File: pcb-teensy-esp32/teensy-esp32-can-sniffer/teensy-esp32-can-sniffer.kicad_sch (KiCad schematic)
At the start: 21 parts, among them J1 Conn_01x04, U1 Seeed_Studio_XIAO_ESP32S3, U2 Teensy4.0, U3 TJA1051T-3, U4 AP63205WU

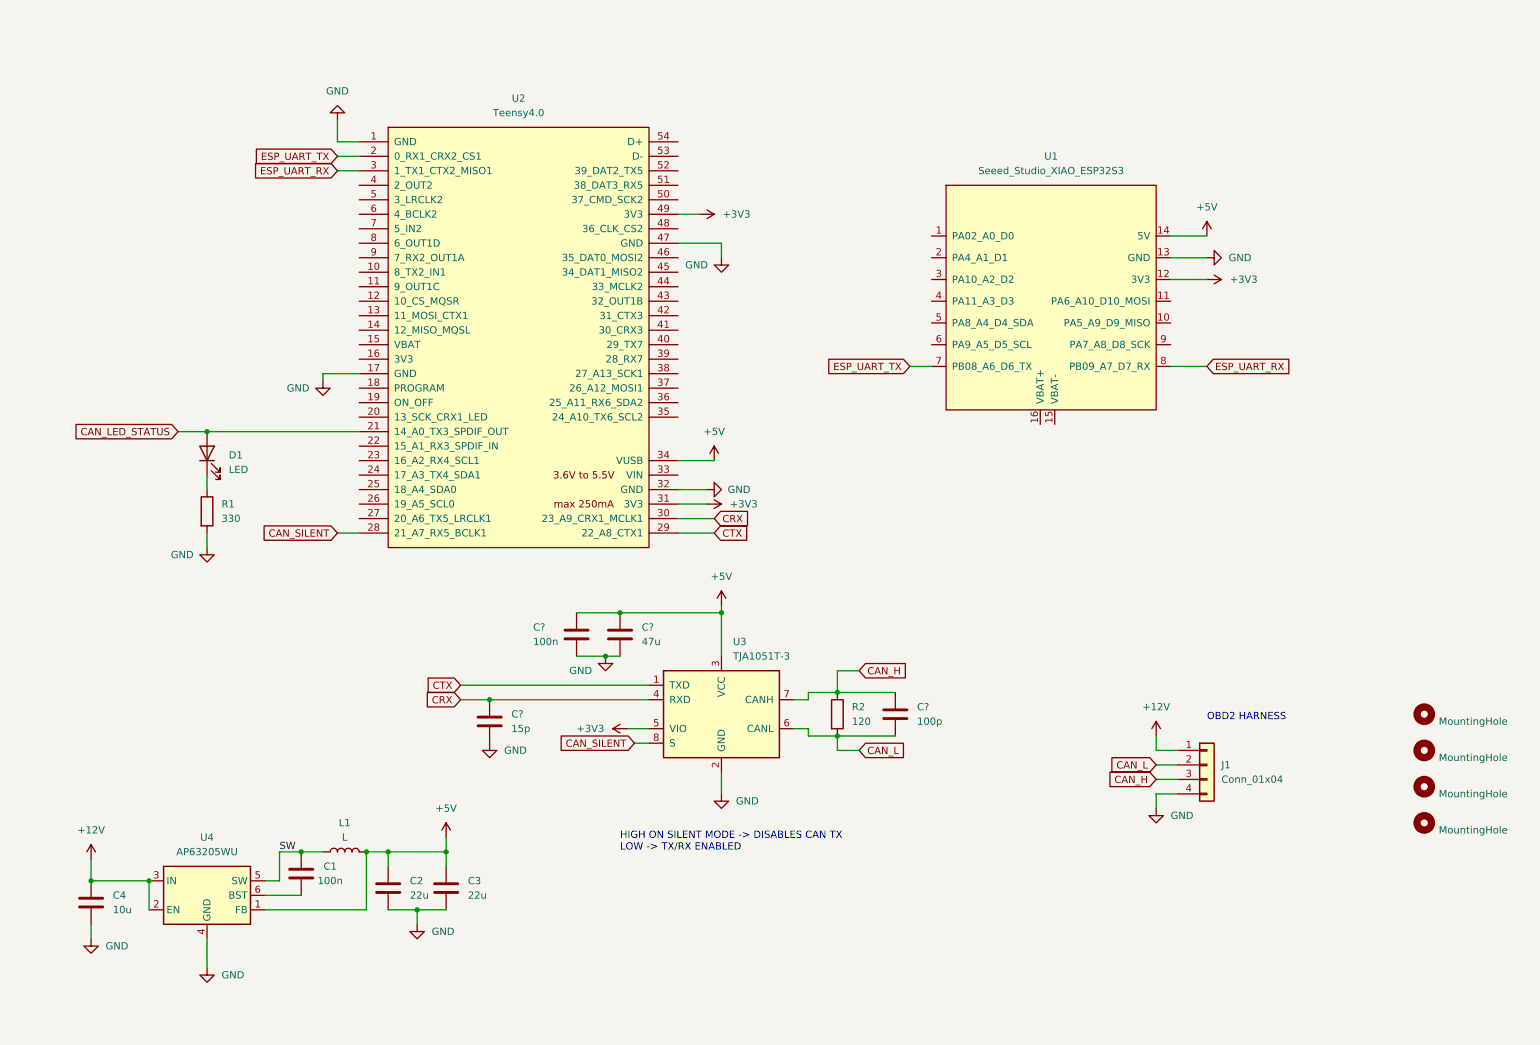
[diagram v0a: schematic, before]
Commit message: Add UI labels and update PCB assets
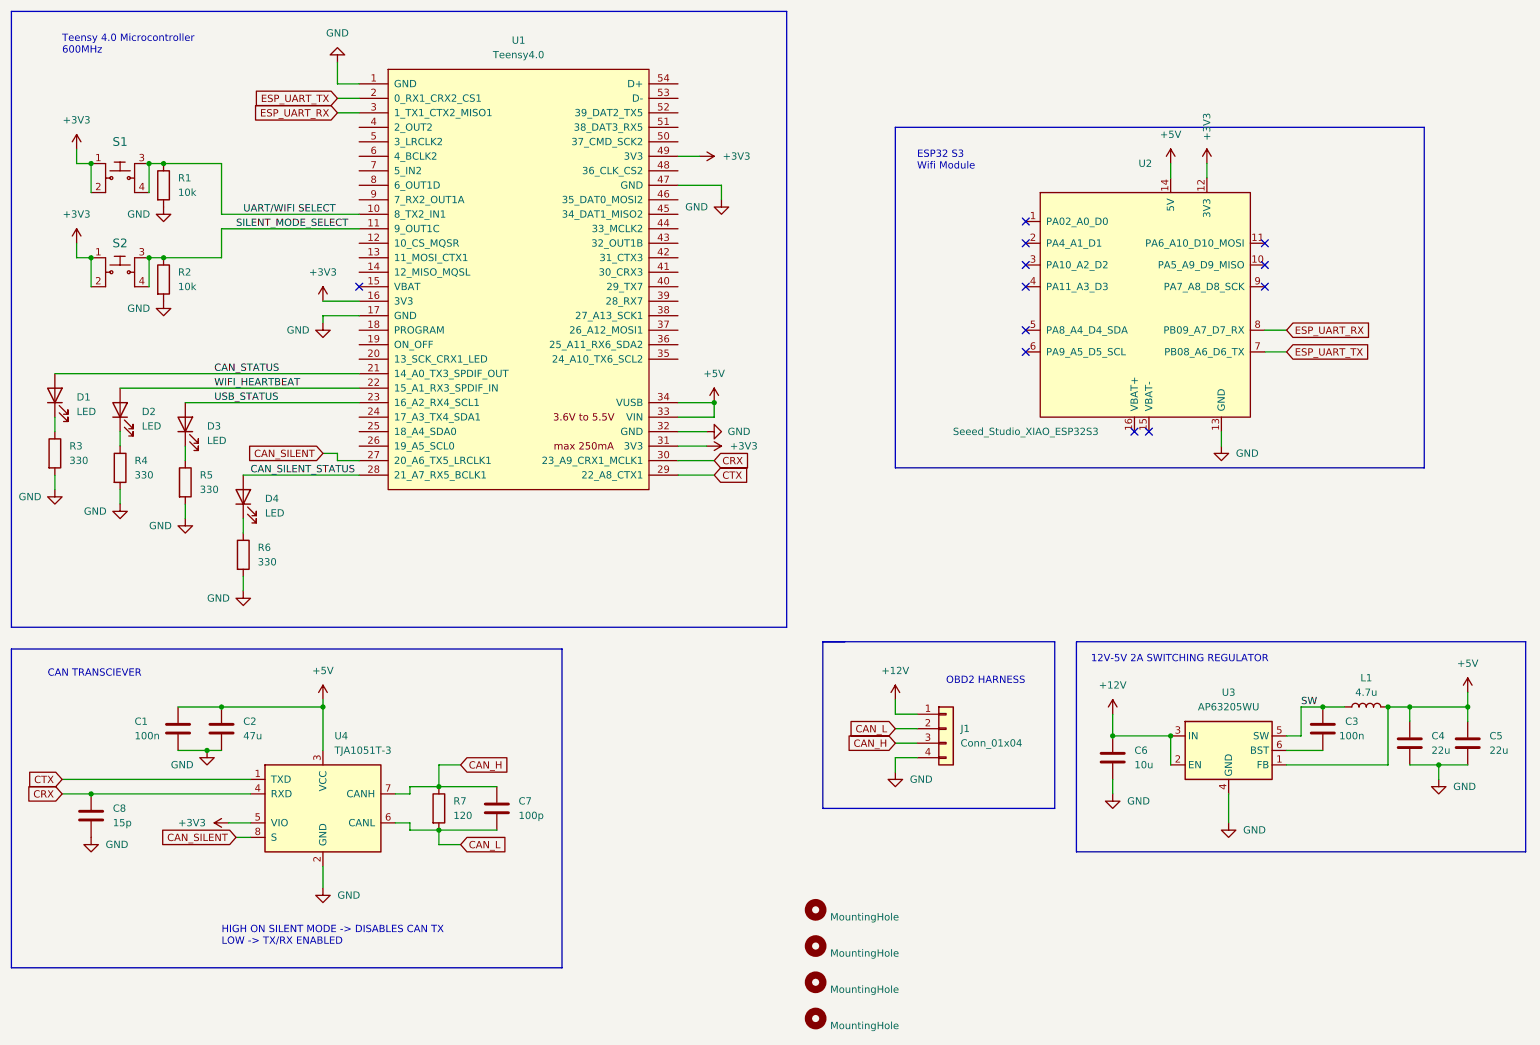
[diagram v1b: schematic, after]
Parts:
- added D2, D3, D4: LED, LED_SMD:LED_0603_1608Metric, symbol Device:LED
- added R1, R2: 10k, Resistor_SMD:R_0603_1608Metric, symbol Device:R
- added R4, R5, R6: 330, Resistor_SMD:R_0603_1608Metric, symbol Device:R
- added S1, S2: PTS645SM43SMTR92_LFS, digikey-footprints:Switch_Tactile_SMD_6x6mm_PTS645, symbol dk_Tactile-Switches:PTS645SM43SMTR92_LFS
- L1: value L -> 4.7u
- gave numbers to parts that had none: 4
- renumbered C1 to C3, C2 to C4, C3 to C5, C4 to C6, R1 to R3, R2 to R7, U2 to U1, U1 to U2, U4 to U3, U3 to U4
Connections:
- net +3V3: now also U1.16 (3V3), S1.1, S1.2, S2.1, S2.2
- net +5V: now also U1.33 (VIN)
- net CAN_SILENT: now also U1.27 (20_A6_TX5_LRCLK1); no longer U1.28 (21_A7_RX5_BCLK1)
- net GND: now also R1.2, R2.2, R4.2, R5.2, R6.2
- net UART/WIFI SELECT: now reaches U1.10 (8_TX2_IN1)
- net UART/WIFI SELECT: now also R1.1, S1.3, S1.4
- net SILENT_MODE_SELECT: now reaches U1.11 (9_OUT1C)
- net SILENT_MODE_SELECT: now also R2.1, S2.3, S2.4
- net WIFI_HEARTBEAT: now reaches U1.22 (15_A1_RX3_SPDIF_IN)
- net WIFI_HEARTBEAT: now also D2.2 (A)
- net USB_STATUS: now reaches U1.23 (16_A2_RX4_SCL1)
- net USB_STATUS: now also D3.2 (A)
- net CAN_LED_STATUS renamed CAN_STATUS
- new net: D4.1 (K), R6.1
- new net: D2.1 (K), R4.1
- new net: D3.1 (K), R5.1
- new net CAN_SILENT_STATUS: D4.2 (A), U1.28 (21_A7_RX5_BCLK1)
- no-connect marks 0 -> 12
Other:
- note added: "12V-5V 2A SWITCHING REGULATOR"
- note added: "CAN TRANSCIEVER"
- note added: "ESP32 S3 Wifi Module"
- note added: "Teensy 4.0 Microcontroller 600MHz"
- moved on the sheet: C1, C2, C3, C4, C5, C6, C7, C8, D1, J1, L1, R3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
